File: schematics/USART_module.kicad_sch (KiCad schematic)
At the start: 14 parts

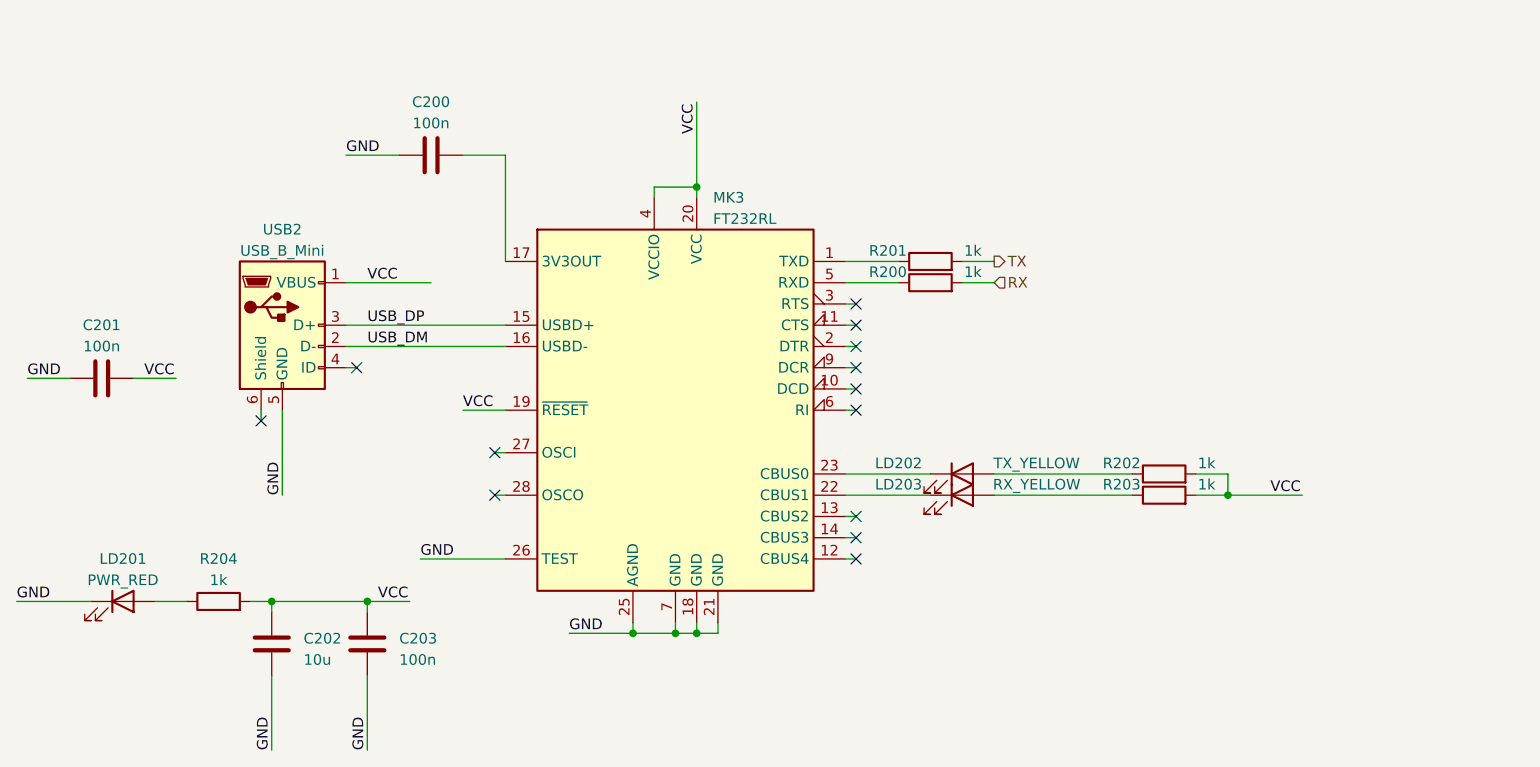
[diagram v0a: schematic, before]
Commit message: Обновил файлы и добавил новые элемнты
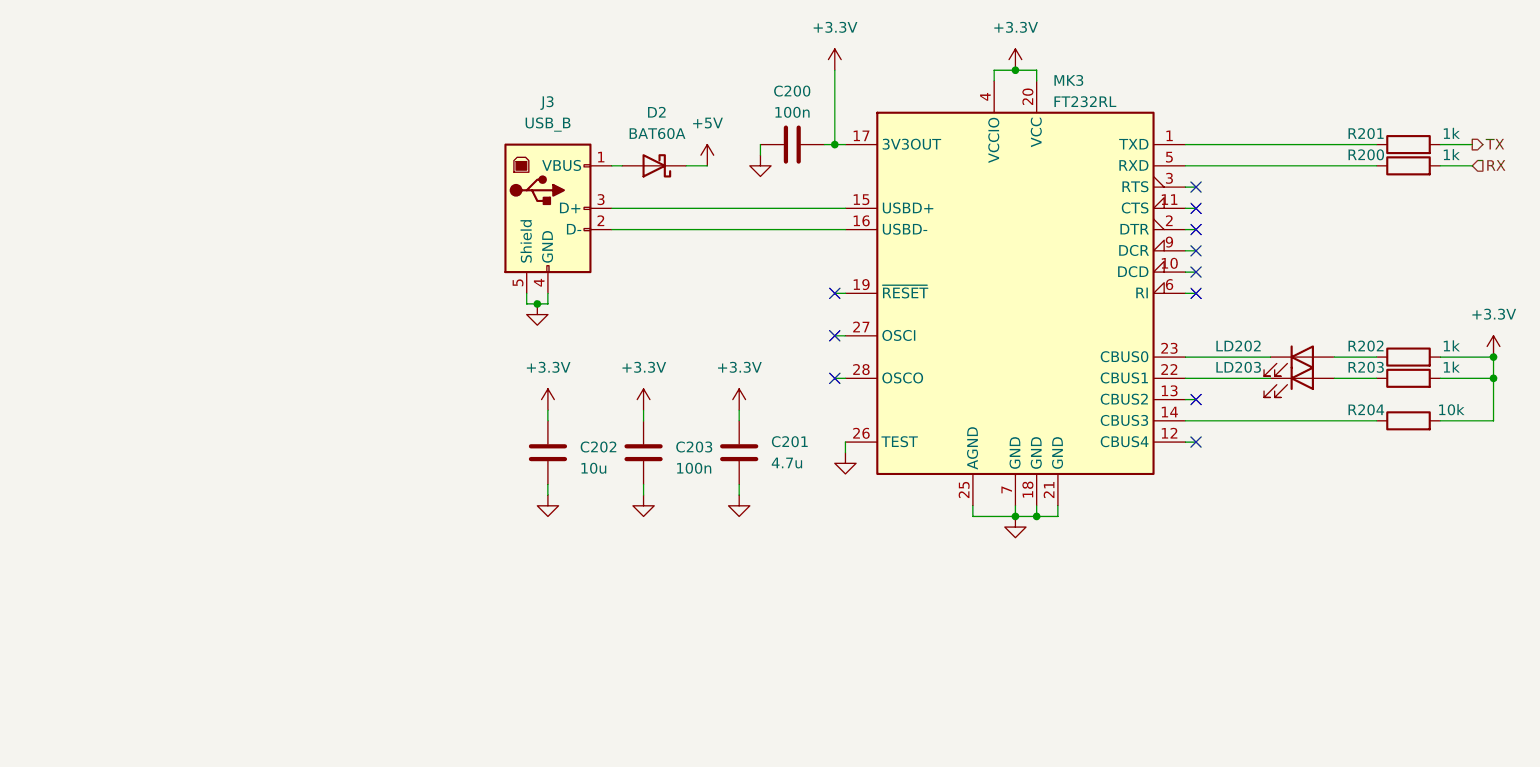
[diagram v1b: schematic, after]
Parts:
- removed LD201: PWR_RED, LED_SMD:LED_1206_3216Metric_Pad1.42x1.75mm_HandSolder, symbol Device:LED
- removed USB2: USB_B_Mini, Connector_USB:USB_Mini-B_Lumberg_2486_01_Horizontal, symbol Connector:USB_B_Mini
- added D2: BAT60A, Diode_SMD:D_SOD-323, symbol Diode:BAT60A
- added J3: USB_B, Connector_USB:USB_B_OST_USB-B1HSxx_Horizontal, symbol Connector:USB_B
- C201: value 100n -> 4.7u
- R204: value 1k -> 10k
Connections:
- net GND: now also J3.4 (GND), J3.5 (Shield)
- net at R204.1: now also MK3.14 (CBUS3)
- net +3.3V: now reaches C200.2, MK3.17 (3V3OUT)
- net +3.3V: now also C201.2, C202.2, C203.2, MK3.20 (VCC), MK3.4 (VCCIO), R202.2, R203.2, R204.2
- net USB_DM: no longer names the net of MK3.16 (USBD-)
- net USB_DM: now also J3.2 (D-)
- net USB_DP: no longer names the net of MK3.15 (USBD+)
- net USB_DP: now also J3.3 (D+)
- removed net VCC: C201.2, C202.2, C203.2, MK3.19 (~{RESET}), MK3.20 (VCC), MK3.4 (VCCIO), R202.2, R203.2, R204.2
- new net: D2.2 (A), J3.1 (VBUS)
- new net +5V: D2.1 (K)
- no-connect marks 13 -> 11
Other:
- moved on the sheet: C200, C201, C202, C203, LD202, LD203, MK3, R200, R201, R202, R203
